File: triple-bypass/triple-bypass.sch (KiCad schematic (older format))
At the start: 68 parts, among them CON101 MD-90SM, J101 HDR1X2, J102 HDR1X3, U101 THS7374IPWR, U102 LMV358M8G-13

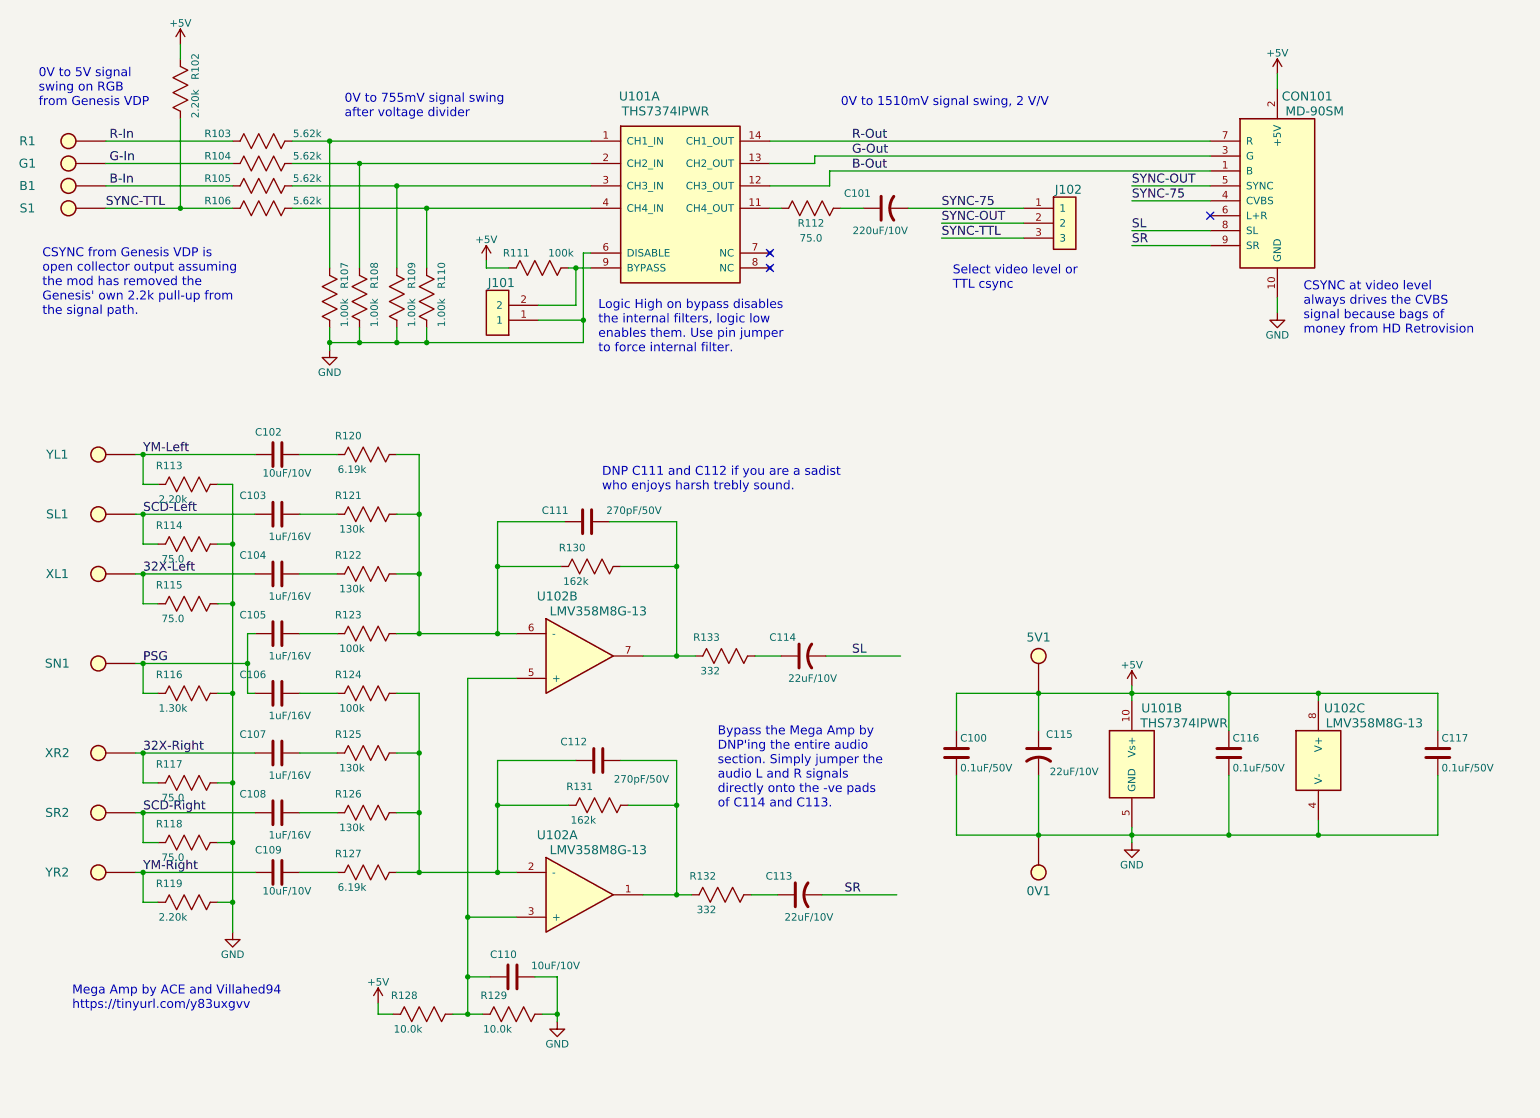
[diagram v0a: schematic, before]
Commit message: changed csync routing to pins 1/14 on 7374
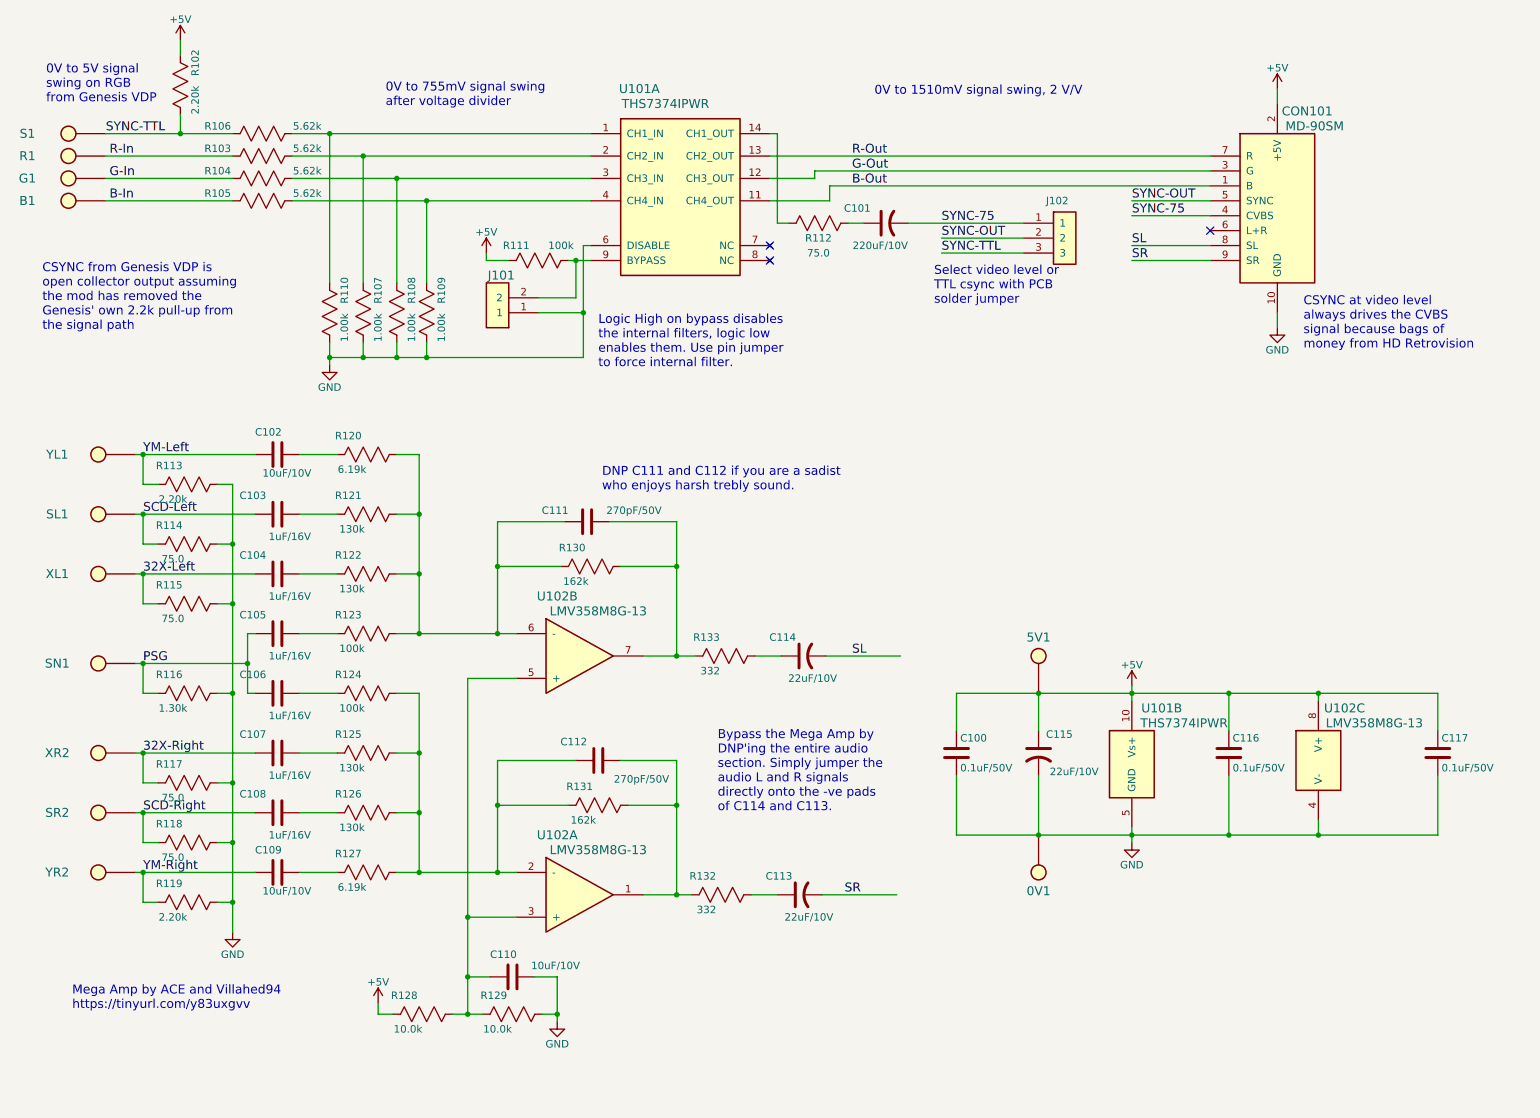
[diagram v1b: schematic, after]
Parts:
- removed J102: HDR1X3, db-thparts:HDR1X3, symbol HDR1X3
- added J102: JMP-PCB-3POS, db-smt:JMP-PCB-3POS, symbol JMP-PCB-3POS
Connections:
- net B-Out: now also U101.11 (CH4_OUT); no longer U101.12 (CH3_OUT)
- net G-Out: now also U101.12 (CH3_OUT); no longer U101.13 (CH2_OUT)
- net R-Out: now also U101.13 (CH2_OUT); no longer U101.14 (CH1_OUT)
- net SYNC-75: now also J102.1
- net SYNC-OUT: now also J102.2
- net SYNC-TTL: now also J102.3
- net at R112.2: now also U101.14 (CH1_OUT); no longer U101.11 (CH4_OUT)
- net at R106.1, R110.2: now also U101.1 (CH1_IN); no longer U101.4 (CH4_IN)
- net at R103.1, R107.2: now also U101.2 (CH2_IN); no longer U101.1 (CH1_IN)
- net at R104.1, R108.2: now also U101.3 (CH3_IN); no longer U101.2 (CH2_IN)
- net at R105.1, R109.2: now also U101.4 (CH4_IN); no longer U101.3 (CH3_IN)
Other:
- note added: "CSYNC from Genesis VDP is \nopen collector output assuming \nthe mod has removed the \nGenesis' own 2.2k pull-up from \nthe signal path"
- note added: "Select video level or\nTTL csync with PCB\nsolder jumper"
- note removed: "CSYNC from Genesis VDP is \nopen collector output assuming \nthe mod has removed the \nGenesis' own 2.2k pull-up from \nthe signal path."
- note removed: "Select video level or\nTTL csync"
- moved on the sheet: B1, C101, CON101, G1, J101, R1, R102, R103, R104, R105, R106, R107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

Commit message: Update to Mega Amp 2.0 and generated 3 seperated BOMs/SCH
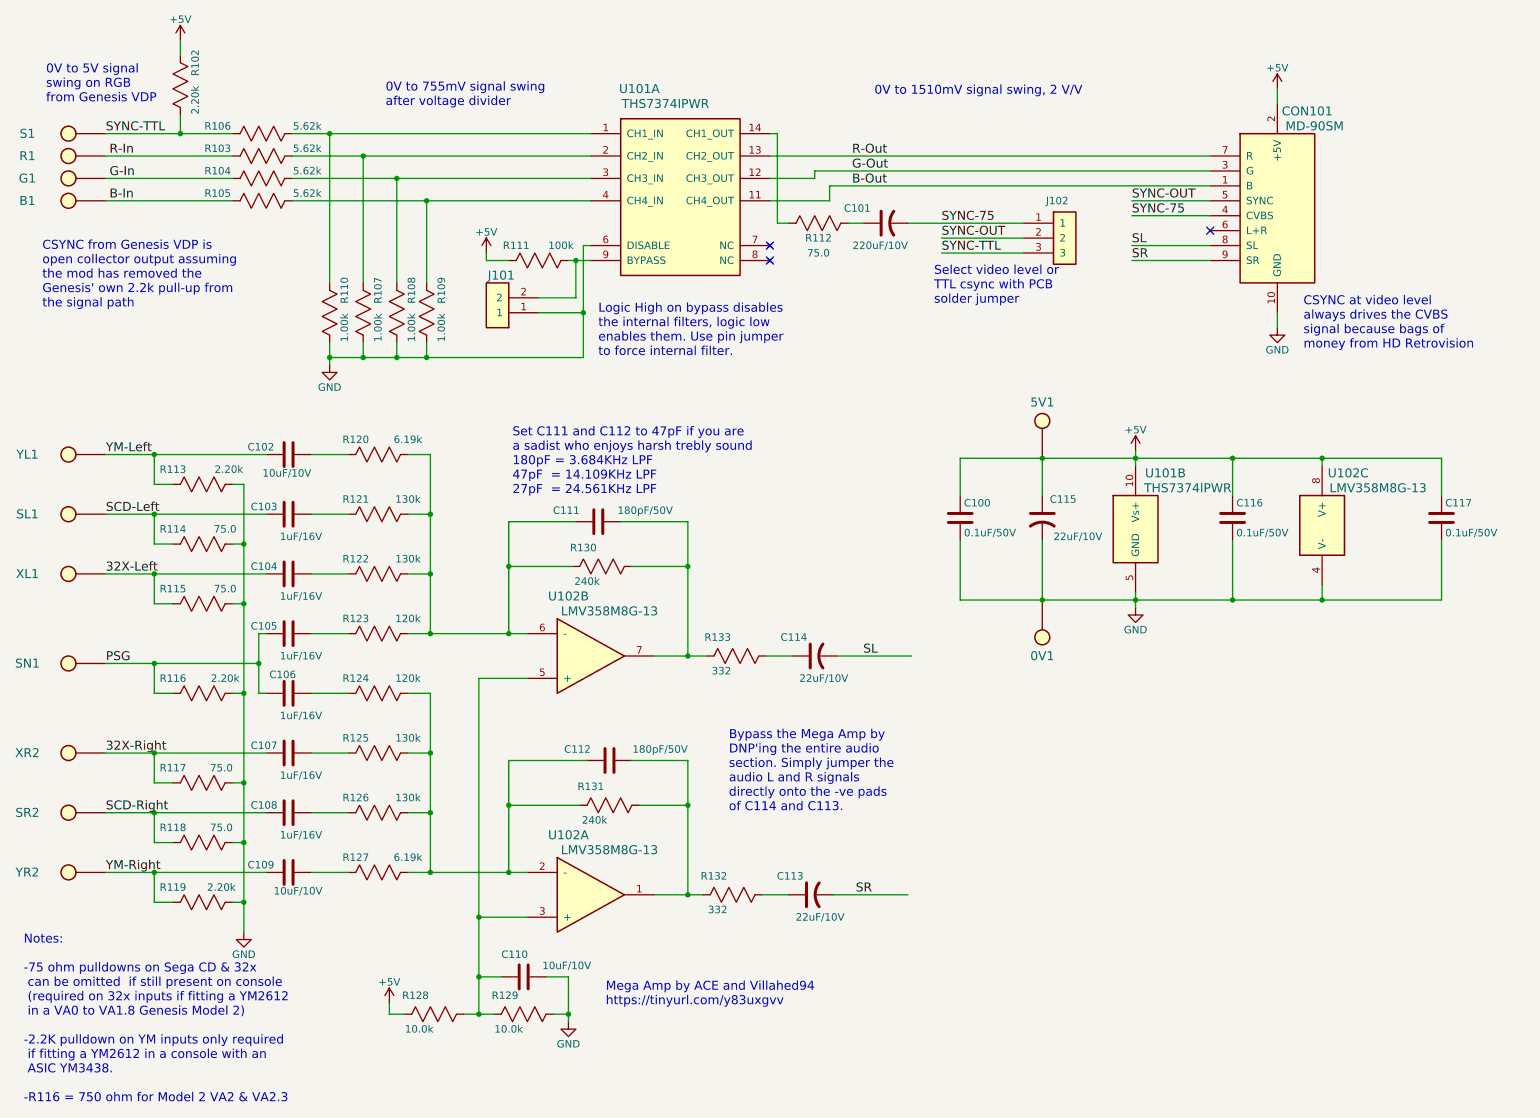
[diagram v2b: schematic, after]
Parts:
- C111, C112: value 270pF/50V -> 180pF/50V; Description CAP CER 270PF 50V X7R 0603 -> CAP CER 180PF 50V X7R 0603; Digikey 1276-2019-1-ND -> 311-4096-6-ND
- R116: value 1.30k -> 2.20k; Description RES 1.30K OHM 1/10W 1% 0603 SMD -> RES 2.20K OHM 1/10W 1% 0603 SMD; Digikey P1.30KHCT-ND -> P2.20KHCT-ND
- R123, R124: value 100k -> 120k; Description RES 100K OHM 1/10W 1% 0603 SMD -> RES 120K OHM 1/10W 1% 0603 SMD; Digikey P100KHCT-ND -> P120KHCT-ND
- R130, R131: value 162k -> 240k; Description RES 162K OHM 1/10W 1% 0603 SMD -> RES 240K OHM 1/10W 1% 0603 SMD; Digikey P162KHCT-ND -> P240KHCT-ND
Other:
- note added: "Notes:\n\n-75 ohm pulldowns on Sega CD & 32x \n can be omitted if still present on console\n (required on 32x inputs if fitting a YM2612 \n in a VA0 to VA1.8 Genesis Model 2)\n\n-2.2K pulldown on YM inputs only required\n if fitting a YM2612 in a console with an \n ASIC YM3438.\n\n-R116 = 750 ohm for Model 2 VA2 & VA2.3"
- note added: "Set C111 and C112 to 47pF if you are \na sadist who enjoys harsh trebly sound\n180pF = 3.684KHz LPF\n47pF = 14.109KHz LPF\n27pF = 24.561KHz LPF"
- note removed: "DNP C111 and C112 if you are a sadist \nwho enjoys harsh trebly sound."
- moved on the sheet: 0V1, 5V1, C100, C102, C103, C104, C105, C106, C107, C108, C109, C110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
